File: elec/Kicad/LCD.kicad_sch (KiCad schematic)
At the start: 14 parts, among them J5 Conn_01x13_Shielded, Q4 SS8050, U11 MMC5633NJL, U2 BMI160, U8 LTR-303ALS-01

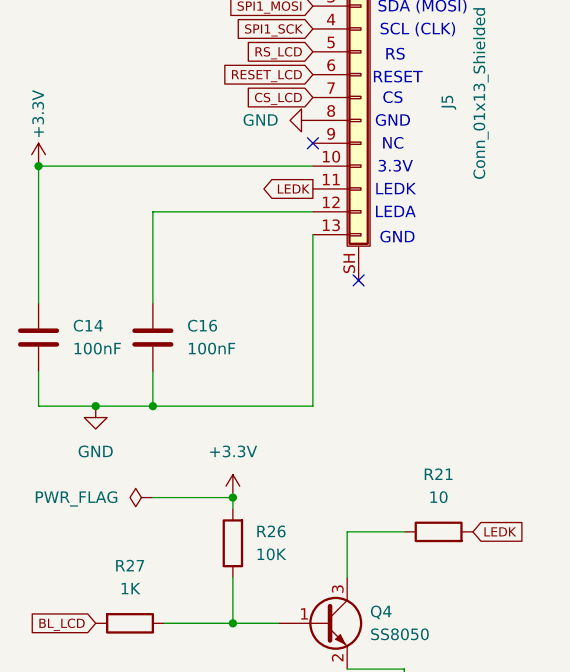
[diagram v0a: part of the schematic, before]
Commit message: ajout d'un Mosfet de type N pour pouvoir gérer le % de batterie (ADC)
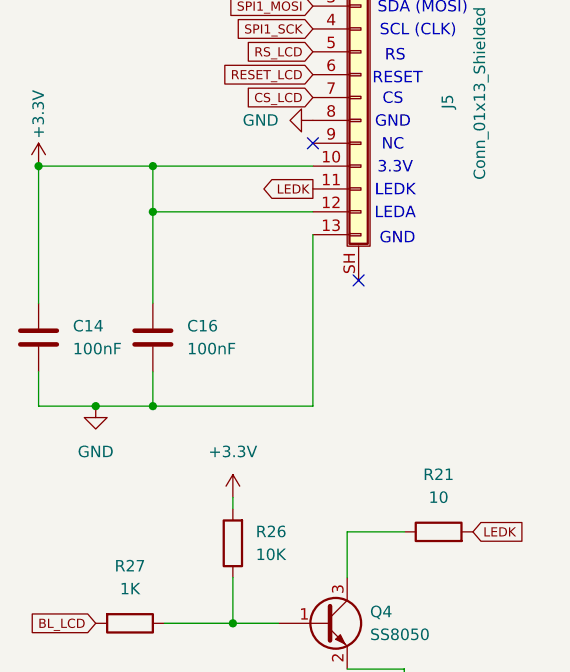
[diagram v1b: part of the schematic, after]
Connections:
- net +3.3V: now also C16.1, J5.12 (Pin_12)
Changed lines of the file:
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@@
-	)
-	(junction
-		(at 52.07 86.36)
-		(diameter 0)
-		(color 0 0 0 0)
 	)
 	(junction
@@
 	)
 	(junction
+		(at 43.18 49.53)
+		(diameter 0)
+		(color 0 0 0 0)
+	)
+	(junction
 		(at 105.41 166.37)
 		(diameter 0)
@@
 	)
 	(junction
+		(at 43.18 54.61)
+		(diameter 0)
+		(color 0 0 0 0)
+	)
+	(junction
 		(at 213.36 123.19)
 		(diameter 0)
@@
 	(wire
 		(pts
-			(xy 30.48 49.53) (xy 60.96 49.53)
+			(xy 30.48 49.53) (xy 43.18 49.53)
 		)
 		(stroke
@@
 	(wire
 		(pts
-			(xy 43.18 86.36) (xy 52.07 86.36)
-		)
-		(stroke
-			(width 0)
-			(type default)
-		)
-	)
-	(wire
-		(pts
 			(xy 52.07 86.36) (xy 52.07 87.63)
 		)
@@
 	(wire
 		(pts
+			(xy 43.18 49.53) (xy 43.18 54.61)
+		)
+		(stroke
+			(width 0)
+			(type default)
+		)
+	)
+	(wire
+		(pts
 			(xy 43.18 72.39) (xy 43.18 76.2)
 		)
@@
 		(pts
 			(xy 64.77 95.25) (xy 64.77 90.17)
+		)
+		(stroke
+			(width 0)
+			(type default)
+		)
+	)
+	(wire
+		(pts
+			(xy 43.18 49.53) (xy 60.96 49.53)
 		)
 		(stroke
@@
 					(unit 1)
 				)
-			)
-		)
-	)
-	(symbol
-		(lib_id "power:PWR_FLAG")
-		(at 43.18 86.36 90)
-		(unit 1)
-		(exclude_from_sim no)
-		(in_bom yes)
-		(on_board yes)
-		(dnp no)
-		(fields_autoplaced yes)
-		(property "Reference" "#FLG01"
-			(at 41.275 86.36 0)
-			(effects
-				(font
-					(size 1.27 1.27)
-				)
-				(hide yes)
-			)
-		)
-		(property "Value" "PWR_FLAG"
-			(at 39.37 86.3599 90)
-			(effects
-				(font
-					(size 1.27 1.27)
-				)
-				(justify left)
-			)
-		)
-		(property "Footprint" ""
-			(at 43.18 86.36 0)
-			(effects
-				(font
-					(size 1.27 1.27)
-				)
-				(hide yes)
-			)
-		)
-		(property "Datasheet" "~"
-			(at 43.18 86.36 0)
-			(effects
-				(font
-					(size 1.27 1.27)
-				)
-				(hide yes)
-			)
-		)
-		(property "Description" "Special symbol for telling ERC where power comes from"
-			(at 43.18 86.36 0)
-			(effects
-				(font
-					(size 1.27 1.27)
-				)
-				(hide yes)
-			)
-		)
-		(pin "1"
-		)
-		(instances
-			(project ""
-				(path "/a1545928-1195-40b9-b3c4-78f837012afb/494e6d32-1eab-4497-b57f-12dbcea47915"
-					(reference "#FLG01")
-					(unit 1)
-				)

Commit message: commencer le PCB vite fait
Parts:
- removed J5: Conn_01x13_Shielded, Connector_FFC-FPC:Hirose_FH12-13S-0.5SH_1x13-1MP_P0.50mm_Horizontal, symbol Connector_Generic_Shielded:Conn_01x13_Shielded
- added J9: Conn_01x13, Connector_FFC-FPC:Hirose_FH12-13S-0.5SH_1x13-1MP_P0.50mm_Horizontal, symbol Connector_Generic:Conn_01x13
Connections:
- net +3.3V: now also J9.10 (Pin_10), J9.12 (Pin_12)
- net CS_LCD: now also J9.7 (Pin_7)
- net GND: now also J9.13 (Pin_13), J9.8 (Pin_8)
- net LEDK: now also J9.11 (Pin_11)
- net RESET_LCD: now also J9.6 (Pin_6)
- net RS_LCD: now also J9.5 (Pin_5)
- net SPI1_MOSI: now also J9.3 (Pin_3)
- net SPI1_SCK: now also J9.4 (Pin_4)
- no-connect marks 12 -> 11
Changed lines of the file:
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@@
-	)
-	(no_connect
-		(at 66.04 62.23)
 	)
 	(no_connect
@@
 	)
 	(symbol
+		(lib_id "Connector_Generic:Conn_01x13")
+		(at 66.04 41.91 0)
+		(unit 1)
+		(exclude_from_sim no)
+		(in_bom yes)
+		(on_board yes)
+		(dnp no)
+		(property "Reference" "J9"
+			(at 73.152 46.228 90)
+			(effects
+				(font
+					(size 1.27 1.27)
+				)
+				(justify left)
+			)
+		)
+		(property "Value" "Conn_01x13"
+			(at 75.184 50.292 90)
+			(effects
+				(font
+					(size 1.27 1.27)
+				)
+				(justify left)
+			)
+		)
+		(property "Footprint" "Connector_FFC-FPC:Hirose_FH12-13S-0.5SH_1x13-1MP_P0.50mm_Horizontal"
+			(at 66.04 41.91 0)
+			(effects
+				(font
+					(size 1.27 1.27)
+				)
+				(hide yes)
+			)
+		)
+		(property "Datasheet" "~"
+			(at 66.04 41.91 0)
+			(effects
+				(font
+					(size 1.27 1.27)
+				)
+				(hide yes)
+			)
+		)
+		(property "Description" "Generic connector, single row, 01x13, script generated (kicad-library-utils/schlib/autogen/connector/)"
+			(at 66.04 41.91 0)
+			(effects
+				(font
+					(size 1.27 1.27)
+				)
+				(hide yes)
+			)
+		)
+		(pin "9"
+		)
+		(pin "6"
+		)
+		(pin "5"
+		)
+		(pin "2"
+		)
+		(pin "13"
+		)
+		(pin "11"
+		)
+		(pin "1"
+		)
+		(pin "8"
+		)
+		(pin "4"
+		)
+		(pin "10"
+		)
+		(pin "12"
+		)
+		(pin "3"
+		)
+		(pin "7"
+		)
+		(instances
+			(project ""
+				(path "/a1545928-1195-40b9-b3c4-78f837012afb/494e6d32-1eab-4497-b57f-12dbcea47915"
+					(reference "J9")
+					(unit 1)
+				)
+			)
+		)
+	)
+	(symbol
 		(lib_id "power:GND")
 		(at 71.12 110.49 0)
@@
 					(unit 1)
 				)
-			)
-		)
-	)
-	(symbol
-		(lib_id "Connector_Generic_Shielded:Conn_01x13_Shielded")
-		(at 66.04 41.91 0)
-		(unit 1)
-		(exclude_from_sim no)
-		(in_bom yes)
-		(on_board yes)
-		(dnp no)
-		(property "Reference" "J5"
-			(at 75.946 43.18 90)
-			(effects
-				(font
-					(size 1.27 1.27)
-				)
-				(justify left)
-			)
-		)
-		(property "Value" "Conn_01x13_Shielded"
-			(at 79.502 51.054 90)
-			(effects
-				(font
-					(size 1.27 1.27)
-				)
-				(justify left)
-			)
-		)
-		(property "Footprint" "Connector_FFC-FPC:Hirose_FH12-13S-0.5SH_1x13-1MP_P0.50mm_Horizontal"
-			(at 66.04 41.91 0)
-			(effects
-				(font
-					(size 1.27 1.27)
-				)
-				(hide yes)
-			)
-		)
-		(property "Datasheet" "~"
-			(at 66.04 41.91 0)
-			(effects
-				(font
-					(size 1.27 1.27)
-				)
-				(hide yes)
-			)
-		)
-		(property "Description" "Generic shielded connector, single row, 01x13, script generated (kicad-library-utils/schlib/autogen/connector/)"
-			(at 66.04 41.91 0)
-			(effects
-				(font
-					(size 1.27 1.27)
-				)
-				(hide yes)
-			)
-		)
-		(pin "SH"
-		)
-		(pin "7"
-		)
-		(pin "2"
-		)
-		(pin "11"
-		)
-		(pin "13"
-		)
-		(pin "3"
-		)
-		(pin "12"
-		)
-		(pin "1"
-		)
-		(pin "10"
-		)
-		(pin "8"
-		)
-		(pin "6"
-		)
-		(pin "4"
-		)
-		(pin "5"
-		)
-		(pin "9"
-		)
-		(instances
-			(project "rulerSchematic"
-				(path "/a1545928-1195-40b9-b3c4-78f837012afb/494e6d32-1eab-4497-b57f-12dbcea47915"
-					(reference "J5")
-					(unit 1)
-				)

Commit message: Jpense pas boire jeudi sérieux vue que y'a pas de 5@8
routage du découplage et des CLK
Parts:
- C14, C16, C19, C20, C21, C22: footprint Capacitor_SMD:C_0603_1608Metric_Pad1.08x0.95mm_HandSolder -> Capacitor_SMD:C_0402_1005Metric_Pad0.74x0.62mm_HandSolder
- R21, R26, R27: footprint Resistor_SMD:R_0603_1608Metric_Pad0.98x0.95mm_HandSolder -> Resistor_SMD:R_0402_1005Metric_Pad0.72x0.64mm_HandSolder
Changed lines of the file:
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@@
 			)
 		)
-		(property "Footprint" "Capacitor_SMD:C_0603_1608Metric_Pad1.08x0.95mm_HandSolder"
+		(property "Footprint" "Capacitor_SMD:C_0402_1005Metric_Pad0.74x0.62mm_HandSolder"
 			(at 239.7252 134.62 0)
 			(effects
@@
 			)
 		)
-		(property "Footprint" "Capacitor_SMD:C_0603_1608Metric_Pad1.08x0.95mm_HandSolder"
+		(property "Footprint" "Capacitor_SMD:C_0402_1005Metric_Pad0.74x0.62mm_HandSolder"
 			(at 134.3152 139.7 0)
 			(effects
@@
 			)
 		)
-		(property "Footprint" "Resistor_SMD:R_0603_1608Metric_Pad0.98x0.95mm_HandSolder"
+		(property "Footprint" "Resistor_SMD:R_0402_1005Metric_Pad0.72x0.64mm_HandSolder"
 			(at 53.848 91.44 90)
 			(effects
@@
 			)
 		)
-		(property "Footprint" "Capacitor_SMD:C_0603_1608Metric_Pad1.08x0.95mm_HandSolder"
+		(property "Footprint" "Capacitor_SMD:C_0402_1005Metric_Pad0.74x0.62mm_HandSolder"
 			(at 31.4452 72.39 0)
 			(effects
@@
 			)
 		)
-		(property "Footprint" "Capacitor_SMD:C_0603_1608Metric_Pad1.08x0.95mm_HandSolder"
+		(property "Footprint" "Capacitor_SMD:C_0402_1005Metric_Pad0.74x0.62mm_HandSolder"
 			(at 44.1452 72.39 0)
 			(effects
@@
 			)
 		)
-		(property "Footprint" "Capacitor_SMD:C_0603_1608Metric_Pad1.08x0.95mm_HandSolder"
+		(property "Footprint" "Capacitor_SMD:C_0402_1005Metric_Pad0.74x0.62mm_HandSolder"
 			(at 195.2752 86.36 0)
 			(effects
@@
 			)
 		)
-		(property "Footprint" "Resistor_SMD:R_0603_1608Metric_Pad0.98x0.95mm_HandSolder"
+		(property "Footprint" "Resistor_SMD:R_0402_1005Metric_Pad0.72x0.64mm_HandSolder"
 			(at 40.64 98.552 90)
 			(effects
@@
 			)
 		)
-		(property "Footprint" "Capacitor_SMD:C_0603_1608Metric_Pad1.08x0.95mm_HandSolder"
+		(property "Footprint" "Capacitor_SMD:C_0402_1005Metric_Pad0.74x0.62mm_HandSolder"
 			(at 120.3452 139.7 0)
 			(effects
@@
 			)
 		)
-		(property "Footprint" "Resistor_SMD:R_0603_1608Metric_Pad0.98x0.95mm_HandSolder"
+		(property "Footprint" "Resistor_SMD:R_0402_1005Metric_Pad0.72x0.64mm_HandSolder"
 			(at 74.93 91.948 90)
 			(effects

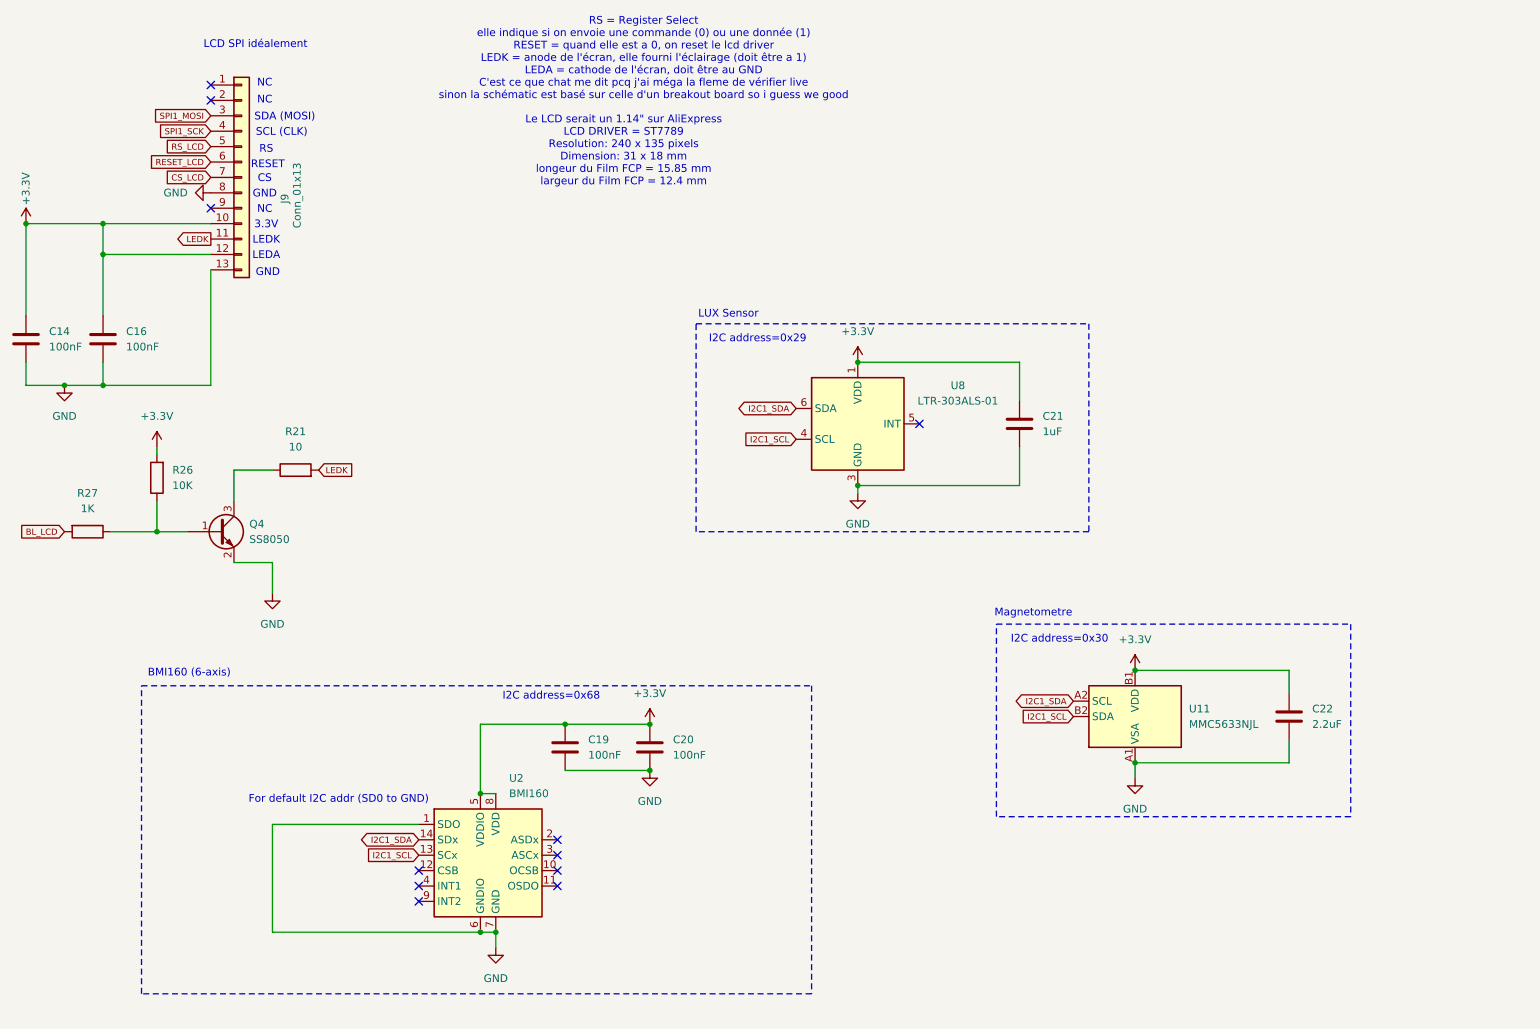
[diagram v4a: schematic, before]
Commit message: modification du magnéto
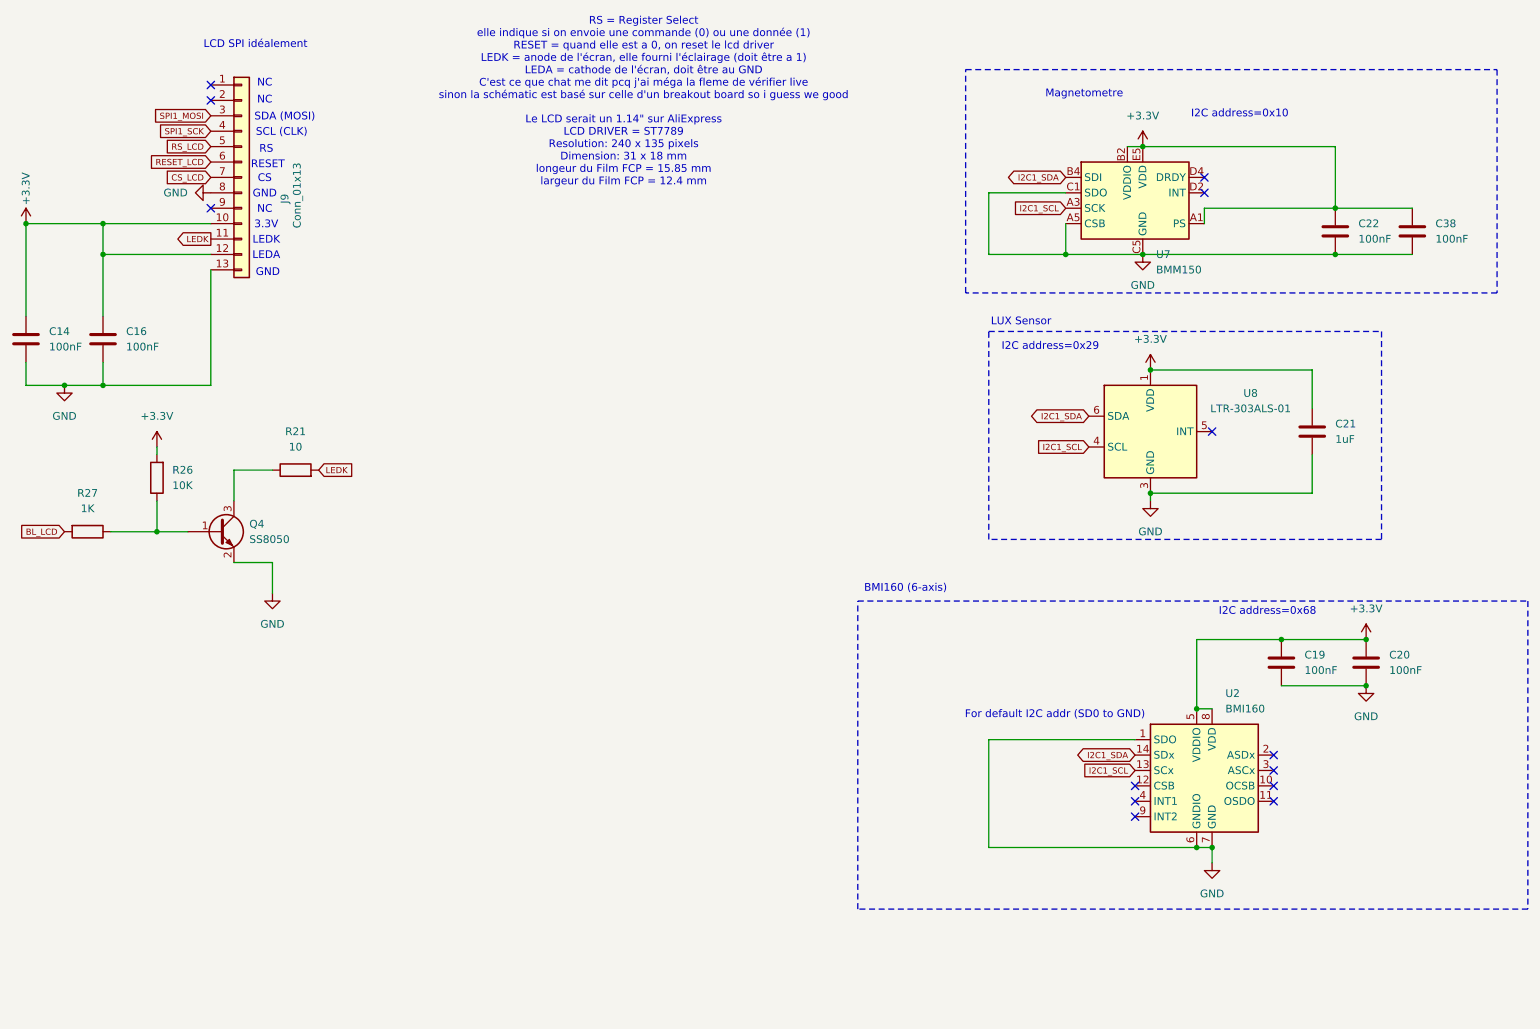
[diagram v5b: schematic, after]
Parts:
- removed U11: MMC5633NJL, Package_BGA:WLP-4_0.86x0.86mm_P0.4mm, symbol Sensor_Magnetic:MMC5633NJL
- added C38: 100nF, Capacitor_SMD:C_0402_1005Metric_Pad0.74x0.62mm_HandSolder, symbol Device:C
- added U7: BMM150, Package_CSP:WLCSP-12_1.56x1.56mm_P0.4mm, symbol Sensor_Magnetic:BMM150
- C22: value 2.2uF -> 100nF
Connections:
- net +3.3V: now also C22.2, C38.2, U7.A1 (PS), U7.B2 (VDDIO), U7.E5 (VDD); no longer C22.1
- net GND: now also C22.1, C38.1, U7.A5 (CSB), U7.C1 (SDO), U7.C5 (GND), U7.E1 (GND), U7.E3 (GND); no longer C22.2
- net I2C1_SCL: now also U7.A3 (SCK)
- net I2C1_SDA: now also U7.B4 (SDI)
- no-connect marks 11 -> 13
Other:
- note added: "I2C address=0x10"
- note removed: "I2C address=0x30"
- moved on the sheet: C19, C20, C21, U2, U8

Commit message: abdel aziz clutch l'app5
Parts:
- removed C22, C38: 100nF, Capacitor_SMD:C_0402_1005Metric_Pad0.74x0.62mm_HandSolder, symbol Device:C
- removed U2: BMI160, Package_LGA:Bosch_LGA-14_3x2.5mm_P0.5mm, symbol Sensor_Motion:BMI160
- removed U7: BMM150, Package_CSP:WLCSP-12_1.56x1.56mm_P0.4mm, symbol Sensor_Magnetic:BMM150
- added R33: 10K, Resistor_SMD:R_0402_1005Metric_Pad0.72x0.64mm_HandSolder, symbol Device:R
- added U2: ADXL343BCCZ, LGA_CC-14-1_ADI, symbol ADXL343:ADXL343BCCZ
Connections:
- net +3.3V: now also R33.2, U2.1 (VDD_I/O), U2.12 (SDO/ALT_ADDRESS), U2.6 (VS), U2.7 (*CS)
- net CS_LCD: now also R33.1
- net GND: now also U2.2 (GND), U2.4 (GND), U2.5 (GND)
- net I2C1_SCL: now also U2.14 (SCL/SCLK)
- net I2C1_SDA: now also U2.13 (SDA/SDI/SDIO)
- no-connect marks 13 -> 9
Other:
- note added: "ADXL343BCCZ (3-axis)"
- note added: "I2C address=0x1D"
- note removed: "BMI160 (6-axis)"
- note removed: "For default I2C addr (SD0 to GND)"
- note removed: "I2C address=0x10"
- note removed: "I2C address=0x68"
- note removed: "Magnetometre"
